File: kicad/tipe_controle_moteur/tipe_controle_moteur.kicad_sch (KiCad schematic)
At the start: 12 parts

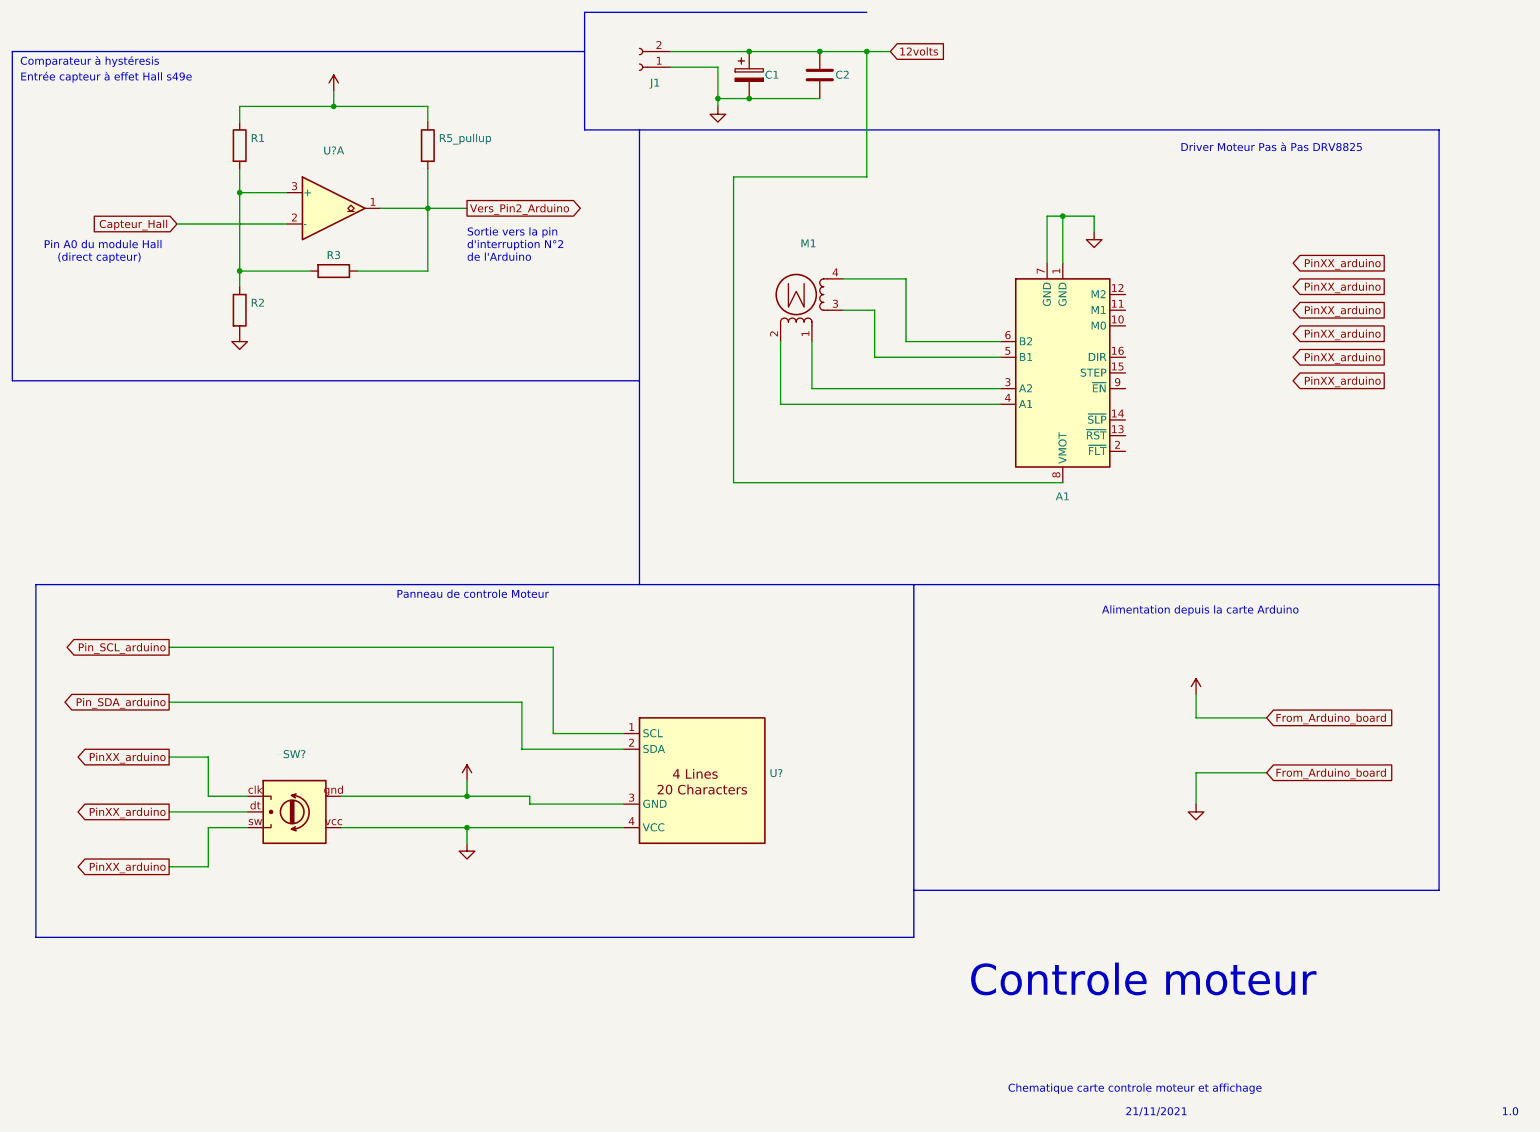
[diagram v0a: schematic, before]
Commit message: changement a cause du logiciel Kicad
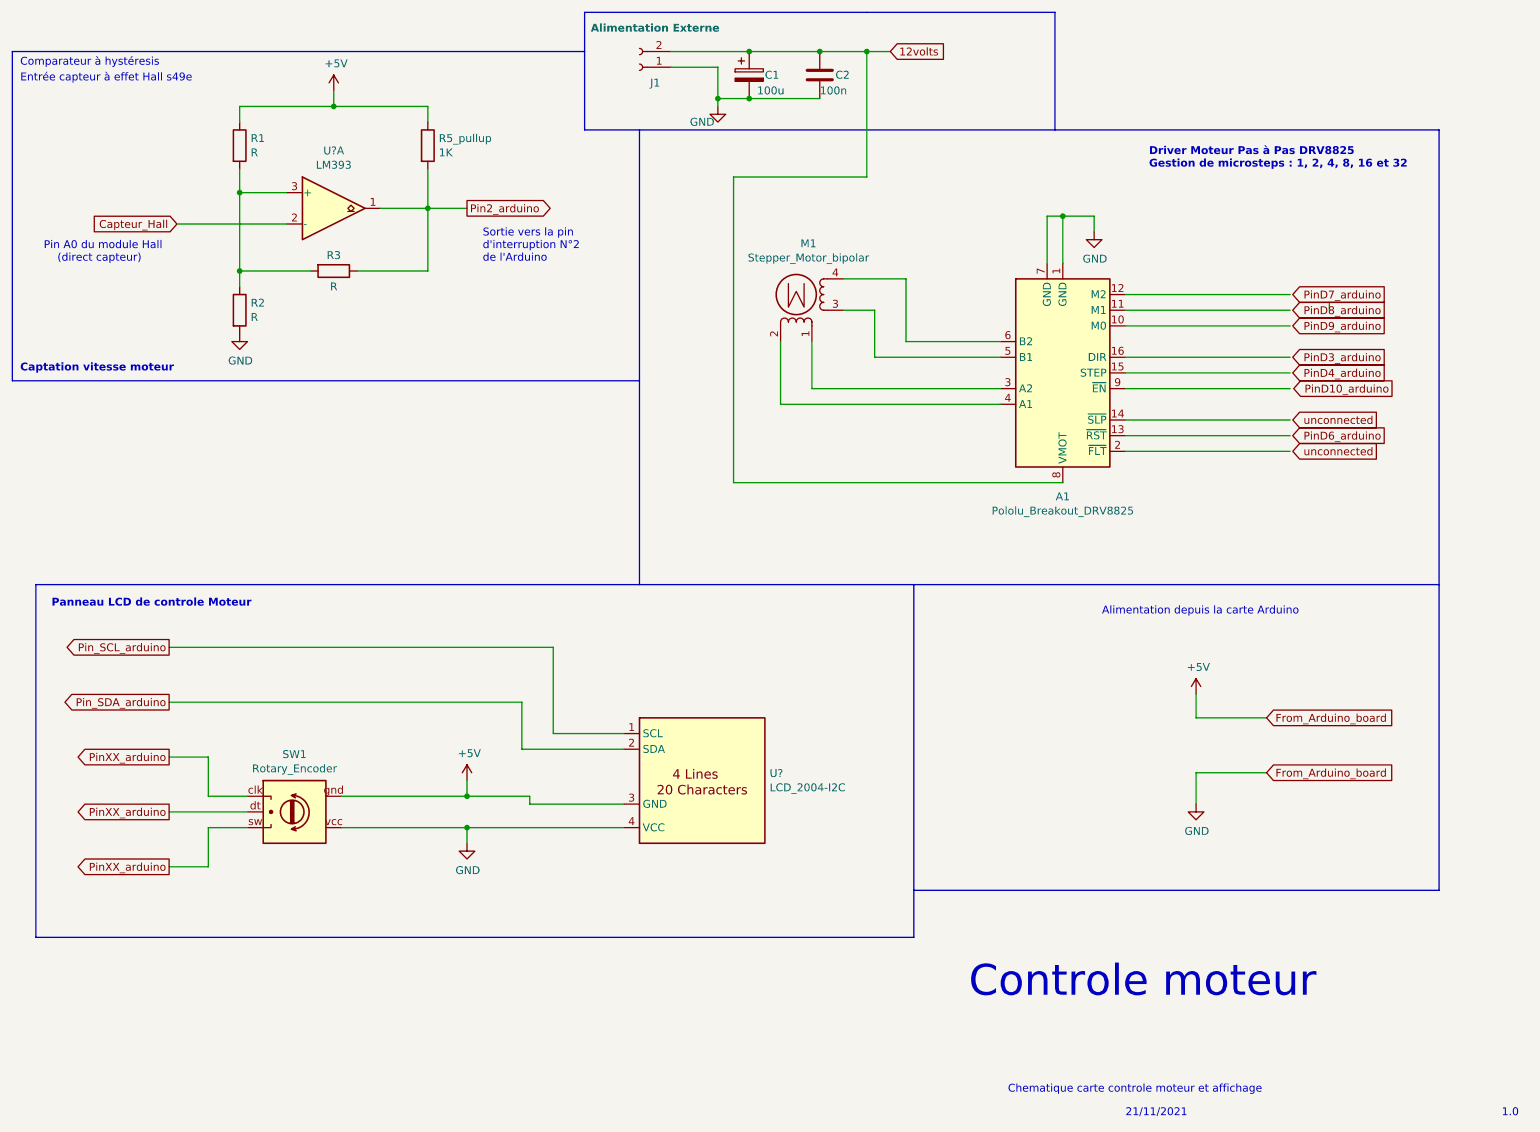
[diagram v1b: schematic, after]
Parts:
- A1: value (none) -> Pololu_Breakout_DRV8825; footprint (none) -> Module:Pololu_Breakout-16_15.2x20.3mm
- C1: value (none) -> 100u
- C2: value (none) -> 100n
- J1: value (none) -> Alimentation Externe
- M1: value (none) -> Stepper_Motor_bipolar
- R1, R2, R3: value (none) -> R
- R5_pullup: value (none) -> 1K
- SW1: renamed from SW?; value (none) -> Rotary_Encoder
- U?: value (none) -> LM393
- U?: value (none) -> LCD_2004-I2C; footprint (none) -> Display:LCD1602-I2C
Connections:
- net Vers_Pin2_Arduino renamed Pin2_arduino
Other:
- note added: "Captation vitesse moteur"
- note added: "Driver Moteur Pas à Pas DRV8825 Gestion de microsteps : 1, 2, 4, 8, 16 et 32"
- note added: "Panneau LCD de controle Moteur"
- note removed: "Driver Moteur Pas à Pas DRV8825"
- note removed: "Panneau de controle Moteur"
